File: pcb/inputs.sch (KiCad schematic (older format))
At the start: 83 parts, among them P90 5v, P92 GND, P93 MAP, U11 MPXA6115AC6U, U4 MAX9926UAEE+, U6 MPXA4250AC6U

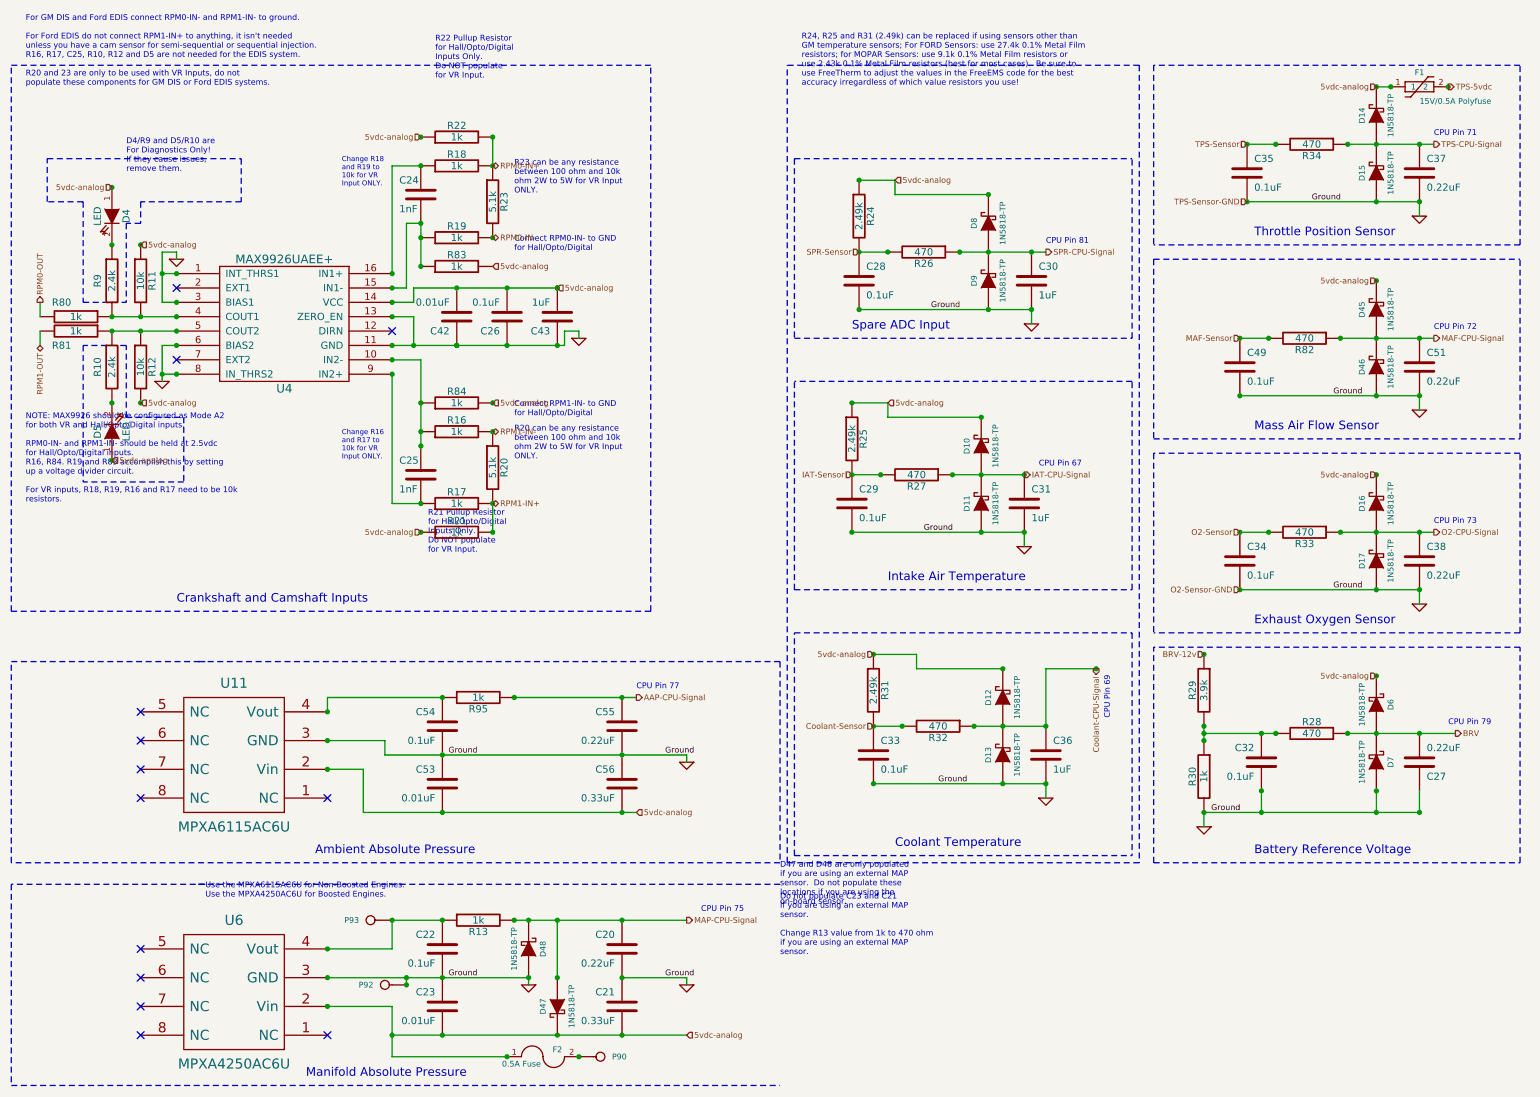
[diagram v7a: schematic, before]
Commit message: Removed polyswitch_smd library as it isn't needed after I changed F1 component to a different type to match F2.
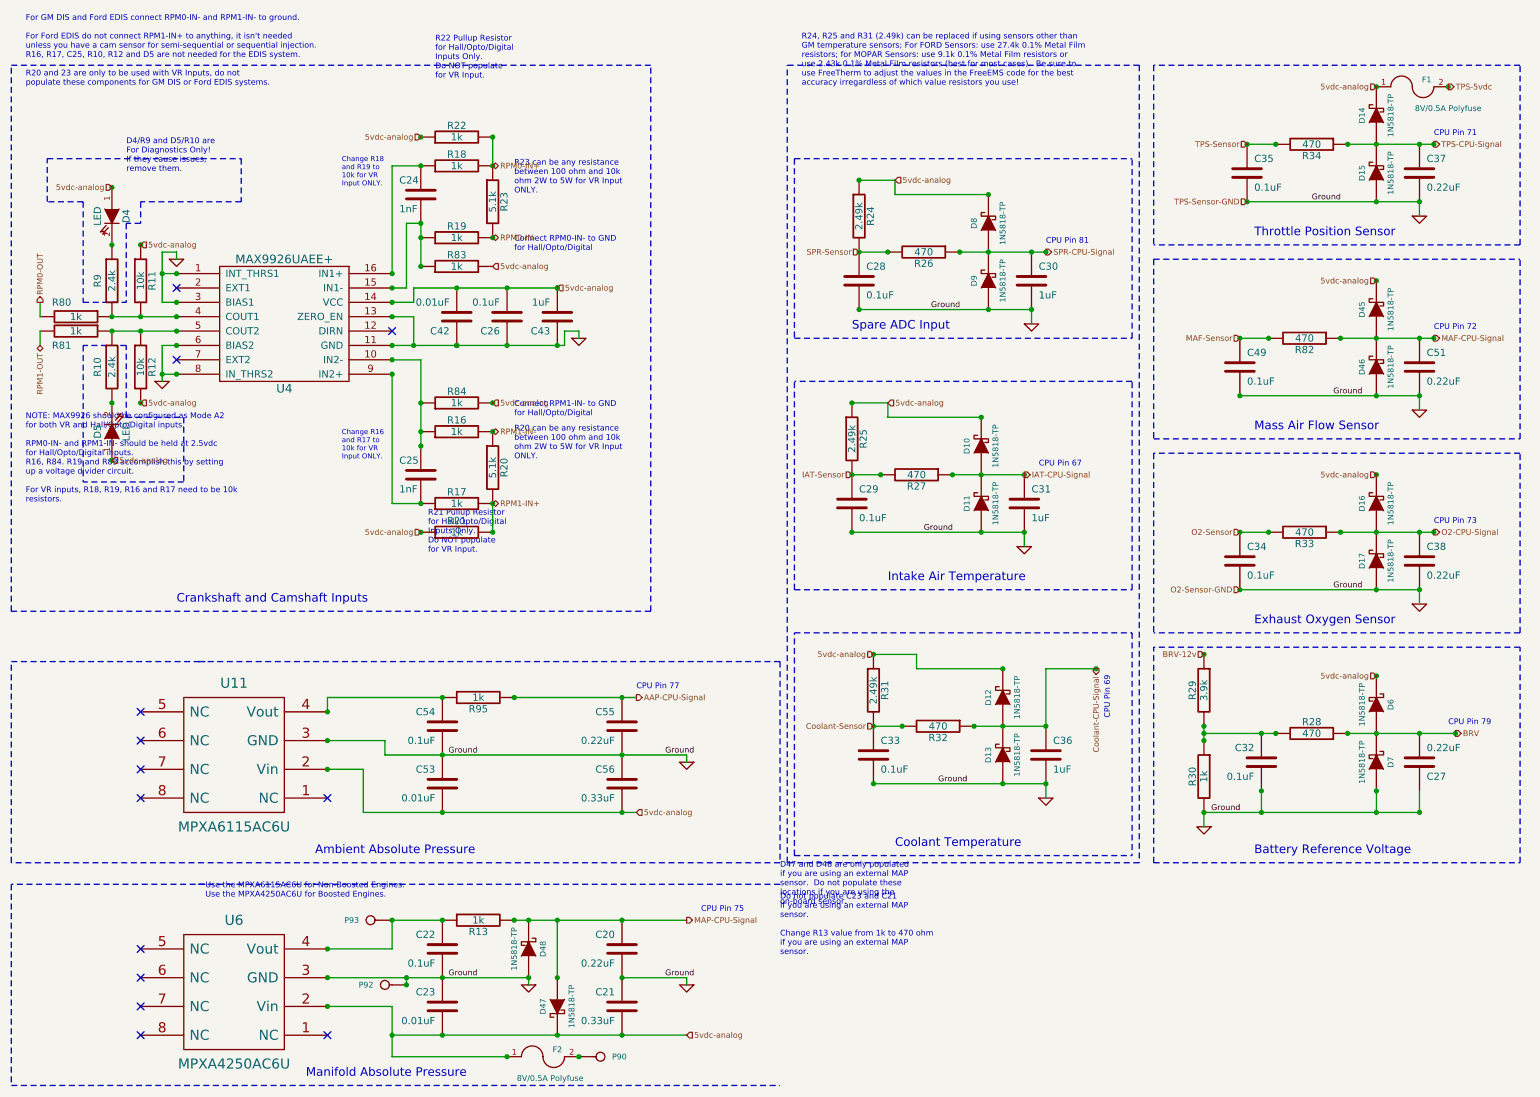
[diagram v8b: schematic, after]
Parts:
- removed F1: 15V/0.5A Polyfuse, symbol SMD
- added F1: 8V/0.5A Polyfuse, symbol FUSE
- F2: value 0.5A Fuse -> 8V/0.5A Polyfuse
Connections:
- net 5vdc-analog: now also F1.1
- net TPS-5vdc: now also F1.2
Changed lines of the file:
@@
-EESchema Schematic File Version 2  date Fri 24 May 2013 09:53:21 PM EDT
+EESchema Schematic File Version 2  date Wed 29 May 2013 06:21:31 PM EDT
 LIBS:opto
 LIBS:power
 LIBS:conn
 LIBS:transistors
-LIBS:polyswitch_smd
 LIBS:device
 LIBS:Jaguar
@@
 Sheet 4 7
 Title "Jaguar PCB for FreeEMS"
-Date "25 may 2013"
+Date "29 may 2013"
 Rev "0.6-alpha"
 Comp "git hash: xxxxxxxxxx"
@@
 Comment4 ""
 $EndDescr
+Connection ~ 7750 1900
+Connection ~ 10600 5250
+Connection ~ 10450 3850
+Connection ~ 10450 2500
+Connection ~ 10450 1150
+Connection ~ 10550 750
+$Comp
+L FUSE F1
+U 1 1 51A67DEA
+P 10300 750
+F 0 "F1" H 10400 800 40  0000 C CNN
+F 1 "8V/0.5A Polyfuse" H 10550 600 40  0000 C CNN
+	1    10300 750
+	1    0    0    -1
+$EndComp
 Connection ~ 4500 7500
 Connection ~ 4000 7500
@@
 Connection ~ 3200 7350
 Wire Wire Line
-	10050 750  10150 750
-Connection ~ 10550 750
-Connection ~ 10150 750
-Wire Wire Line
 	4150 6950 2750 6950
 Connection ~ 2750 6750
@@
 P 4250 7500
 F 0 "F2" H 4350 7550 40  0000 C CNN
-F 1 "0.5A Fuse" H 4100 7450 40  0000 C CNN
+F 1 "8V/0.5A Polyfuse" H 4300 7350 40  0000 C CNN
 	1    4250 7500
 	1    0    0    -1
@@
 	1    0    0    -1
 $EndComp
-$Comp
-L SMD F1
-U 1 1 50D66AB8
-P 10350 750
-F 0 "F1" H 10350 850 40  0000 C CNN
-F 1 "15V/0.5A Polyfuse" H 10600 650 40  0000 C CNN
-	1    10350 750
-	1    0    0    -1
-$EndComp
